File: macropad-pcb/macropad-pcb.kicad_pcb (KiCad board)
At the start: 2 copper layers, 83.3 x 57.2 mm, 34 parts, among them J1 USB_B_Mini, SW1 SW_Push, SW2 SW_Push, SW3 SW_Push, SW4 SW_Push, SW5 SW_Push, SW6 SW_Push, SW7 SW_Push, SW8 SW_Push, SW9 SW_Push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

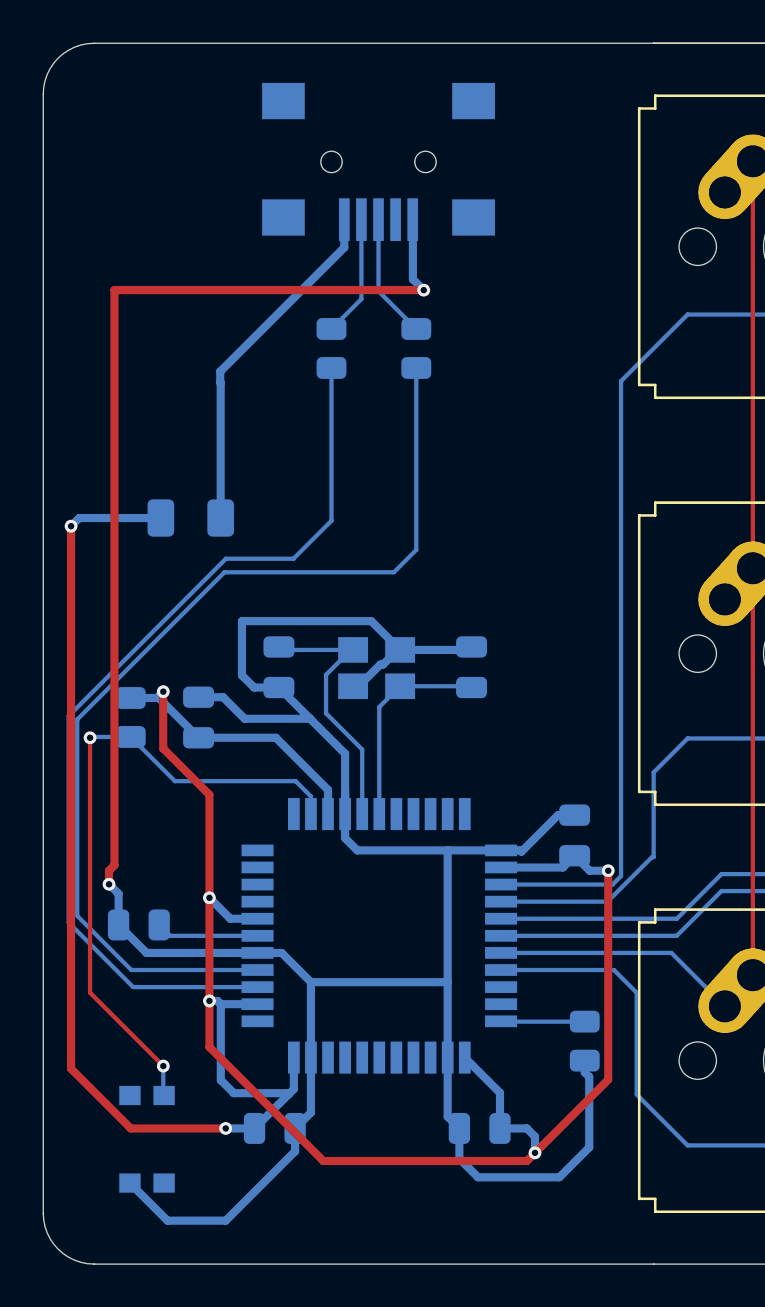
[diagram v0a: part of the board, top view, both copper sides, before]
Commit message: added gnd net fill
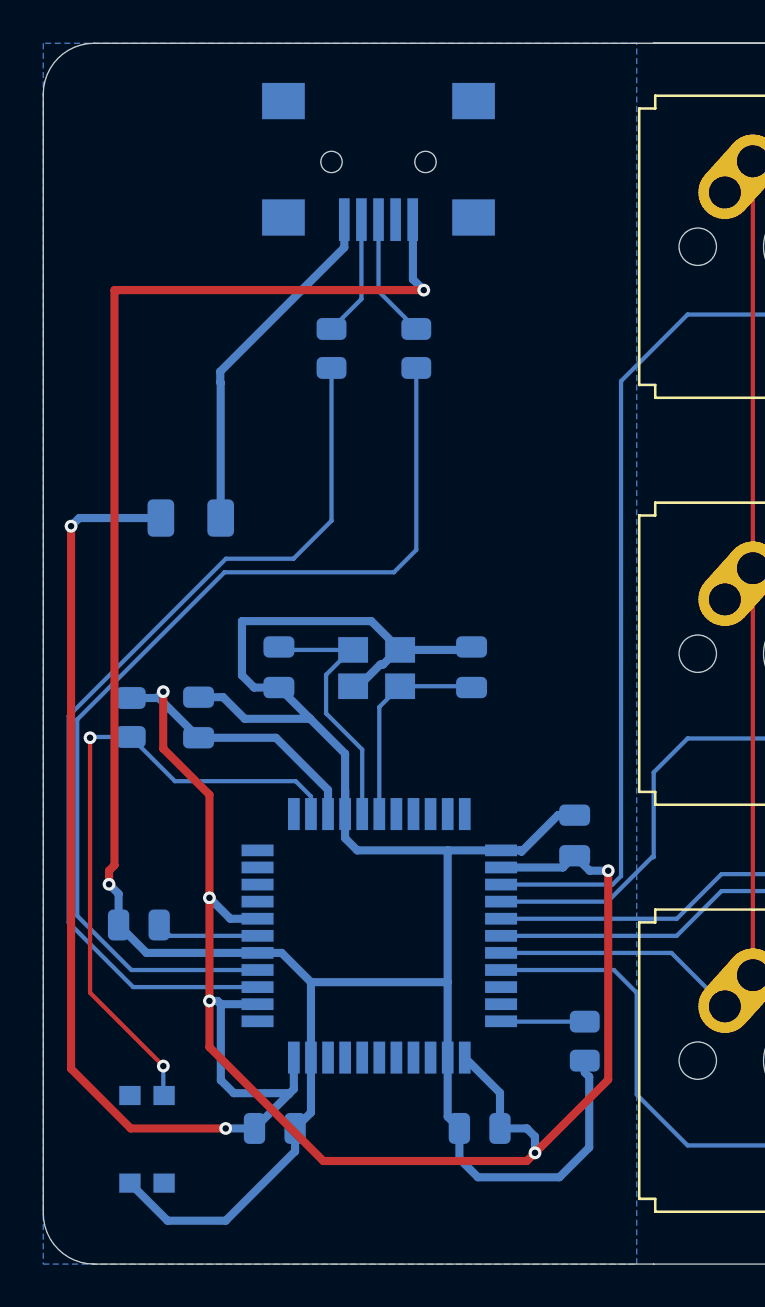
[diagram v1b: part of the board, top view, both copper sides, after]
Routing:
- added copper zone on B.Cu, net GND
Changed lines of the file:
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@@
 		(net 29)
 	)
+	(zone
+		(net 1)
+		(net_name "GND")
+		(layer "B.Cu")
+		(hatch edge 0.5)
+		(connect_pads
+			(clearance 0.5)
+		)
+		(min_thickness 0.25)
+		(filled_areas_thickness no)
+		(fill
+			(thermal_gap 0.5)
+			(thermal_bridge_width 0.5)
+		)
+		(polygon
+			(pts
+				(xy 100.0125 47.625) (xy 72.23125 47.625) (xy 72.23125 104.775) (xy 100.0125 104.775)
+			)
+		)
+	)
 )

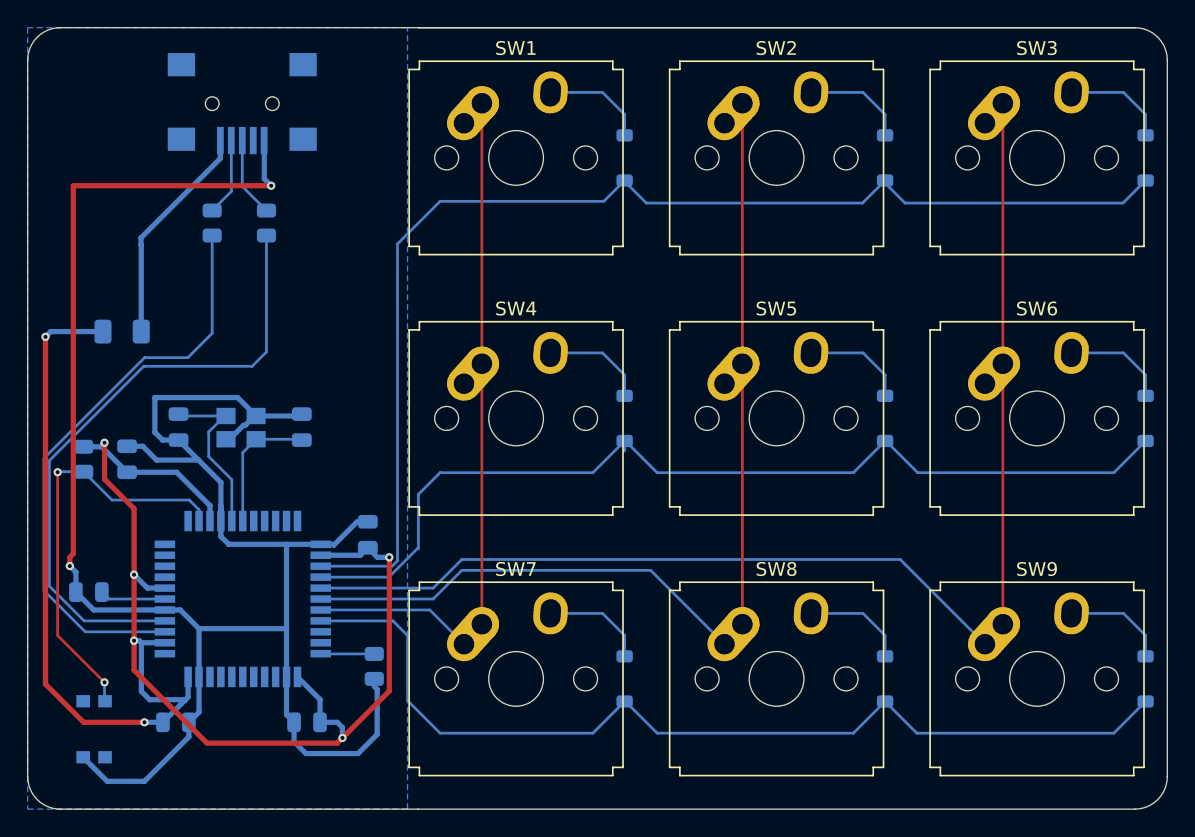
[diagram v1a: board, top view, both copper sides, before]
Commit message: changed to just mx footprint since i haven't figured out how to handle the annular width issue of the hybrid footprint and made output files
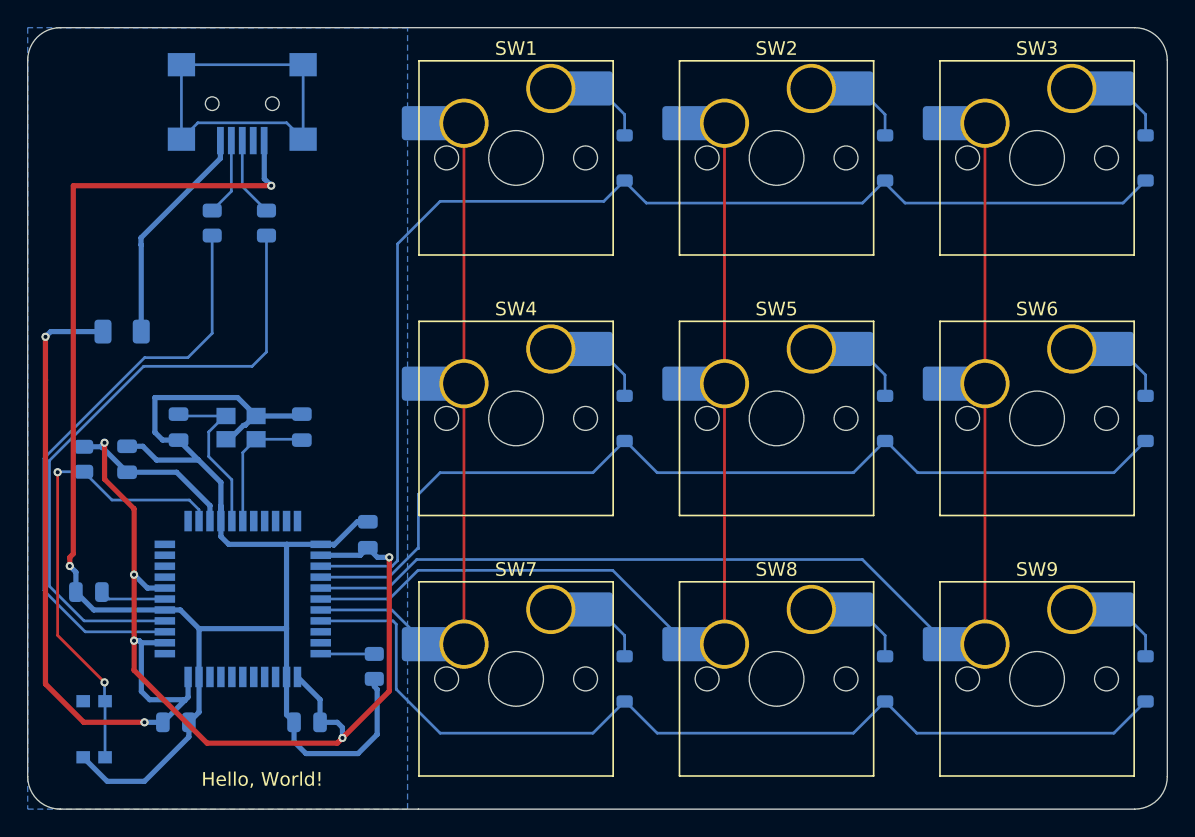
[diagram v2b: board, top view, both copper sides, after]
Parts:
- SW1, SW2, SW3, SW4, SW5, SW6, SW7, SW8, SW9: footprint PCM_Switch_Keyboard_Hybrid:SW_Hybrid_Cherry_MX_Alps_1.00u -> PCM_Switch_Keyboard_Hotswap_Kailh:SW_Hotswap_Kailh_MX_Plated_1.00u
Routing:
- net unconnected-(J1-Shield-Pad6): track 0.00 -> 29.7 mm
- net Net-(U1-~{RESET}): track 30.5 -> 34.6 mm
- net /Col2: track 90.1 -> 87.3 mm
- net /Col0: track 49.6 -> 46.8 mm
- net /Col1: track 70.7 -> 68.0 mm
- net /Row1: track 71.3 -> 70.6 mm
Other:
- outline, holes or cut-outs redrawn
- board text added: "Hello, World!"
